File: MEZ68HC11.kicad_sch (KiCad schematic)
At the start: 22 parts, among them J1 Conn_01x20_Socket, J2 Conn_01x20_Socket, J3 Conn_01x08_Socket, J4 Conn_01x06_Socket, J5 Conn_01x08_Socket, U1 68HC11_PLCC, U2 74HC573, Y1 8MHz

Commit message: add some in the schematics
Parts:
- removed J4: Conn_01x06_Socket, symbol Connector:Conn_01x06_Socket
- added J4: Conn_01x08_Socket, symbol Connector:Conn_01x08_Socket
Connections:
- net GND: now also J4.8 (Pin_8)
- net VCC: now also J4.1 (Pin_1)
- net at RN1.2 (R1), U1.20 (PD0/RX): now also J4.2 (Pin_2)
- net at RN1.3 (R2), U1.21 (PD1/TX): now also J4.3 (Pin_3)
- net at RN1.4 (R3), U1.22 (PD2): now also J4.4 (Pin_4)
- net at RN1.5 (R4), U1.23 (PD3): now also J4.5 (Pin_5)
- net at RN1.6 (R5), U1.24 (PD4): now also J4.6 (Pin_6)
- net at RN1.7 (R6), U1.25 (PD5): now also J4.7 (Pin_7)
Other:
- moved on the sheet: J5, U1

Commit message: Rev001. ordered to JCLPCB
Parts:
- removed U2: 74HC573, symbol 74xx:74LS573
- added U2: 74HC573, Package_DIP:DIP-20_W7.62mm, symbol 0-global:74HC573_rev
- C1, C2, C3: footprint (none) -> Capacitor_THT:C_Disc_D3.0mm_W1.6mm_P2.50mm
- C4, C5: value 0.1uF -> 22pF; footprint (none) -> Capacitor_THT:C_Disc_D3.0mm_W1.6mm_P2.50mm
- C6: footprint (none) -> Capacitor_THT:CP_Radial_D4.0mm_P2.00mm
- J1, J2: footprint (none) -> Connector_PinSocket_2.54mm:PinSocket_1x20_P2.54mm_Vertical
- J3, J4, J5: footprint (none) -> Connector_PinSocket_2.54mm:PinSocket_1x08_P2.54mm_Vertical
- JP1, JP2, JP3: footprint (none) -> Jumper:SolderJumper-2_P1.3mm_Open_RoundedPad1.0x1.5mm
- R1, R2: footprint (none) -> Resistor_THT:R_Axial_DIN0204_L3.6mm_D1.6mm_P7.62mm_Horizontal
- U1: footprint (none) -> Package_LCC:PLCC-52
- Y1: footprint (none) -> Crystal:Crystal_HC49-U_Vertical
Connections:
- net A0: now also U2.12 (Q7)
- net A1: now also U2.13 (Q6)
- net A2: now also U2.14 (Q5)
- net A3: now also U2.15 (Q4)
- net A4: now also U2.16 (Q3)
- net A5: now also U2.17 (Q2)
- net A6: now also U2.18 (Q1)
- net A7: now also U2.19 (Q0)
- net D0: now also RN3.9 (R8), U2.9 (D7); no longer RN3.2 (R1)
- net D1: now also RN3.8 (R7), U2.8 (D6); no longer RN3.3 (R2)
- net D2: now also RN3.7 (R6), U2.7 (D5); no longer RN3.4 (R3)
- net D3: now also RN3.6 (R5), U2.6 (D4); no longer RN3.5 (R4)
- net D4: now also RN3.5 (R4), U2.5 (D3); no longer RN3.6 (R5)
- net D5: now also RN3.4 (R3), U2.4 (D2); no longer RN3.7 (R6)
- net D6: now also RN3.3 (R2), U2.3 (D1); no longer RN3.8 (R7)
- net D7: now also RN3.2 (R1), U2.2 (D0); no longer RN3.9 (R8)
- net GND: now also U2.1 (OE), U2.10 (GND)
- net PA0: now also RN2.9 (R8); no longer RN2.7 (R6)
- net PA2: now also RN2.7 (R6); no longer RN2.9 (R8)
- net VCC: now also U2.20 (VCC)
- net at U1.4 (AS): now also U2.11 (Load)

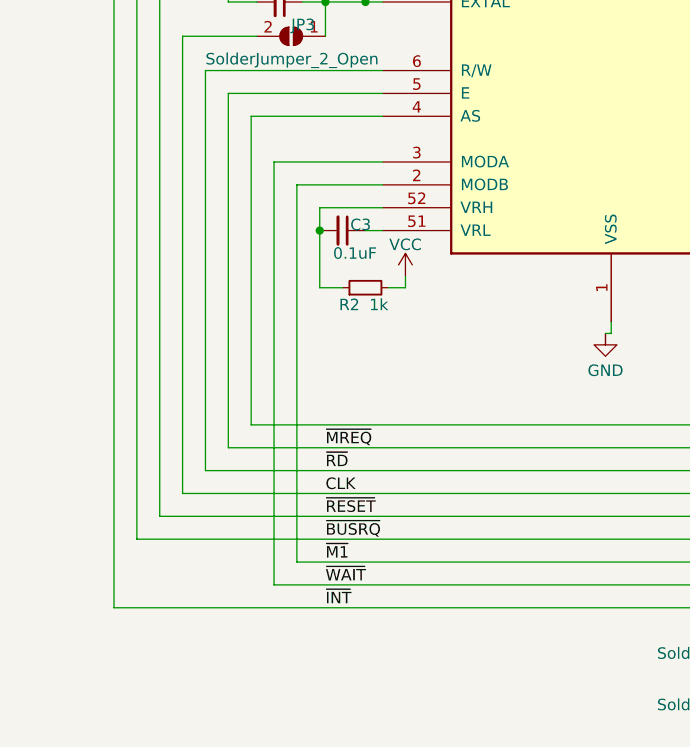
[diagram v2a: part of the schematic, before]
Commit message: add 4.7k between MODA and PIC
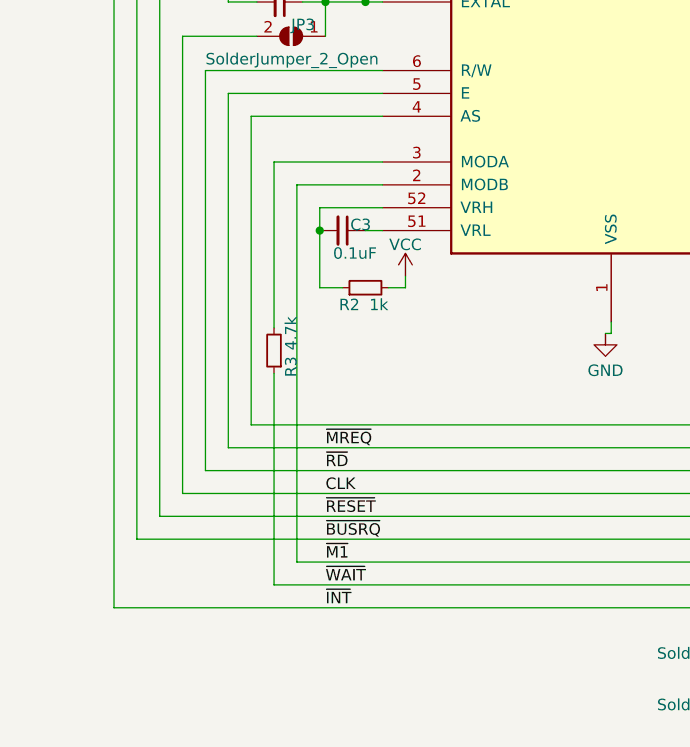
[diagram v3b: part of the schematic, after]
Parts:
- added R3: 4.7k, Resistor_THT:R_Axial_DIN0204_L3.6mm_D1.6mm_P7.62mm_Horizontal, symbol Device:R_Small
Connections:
- net ~{WAIT}: now also R3.1; no longer U1.3 (MODA)
- new net: R3.2, U1.3 (MODA)
